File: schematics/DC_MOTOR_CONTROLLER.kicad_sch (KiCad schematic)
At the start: 0 parts

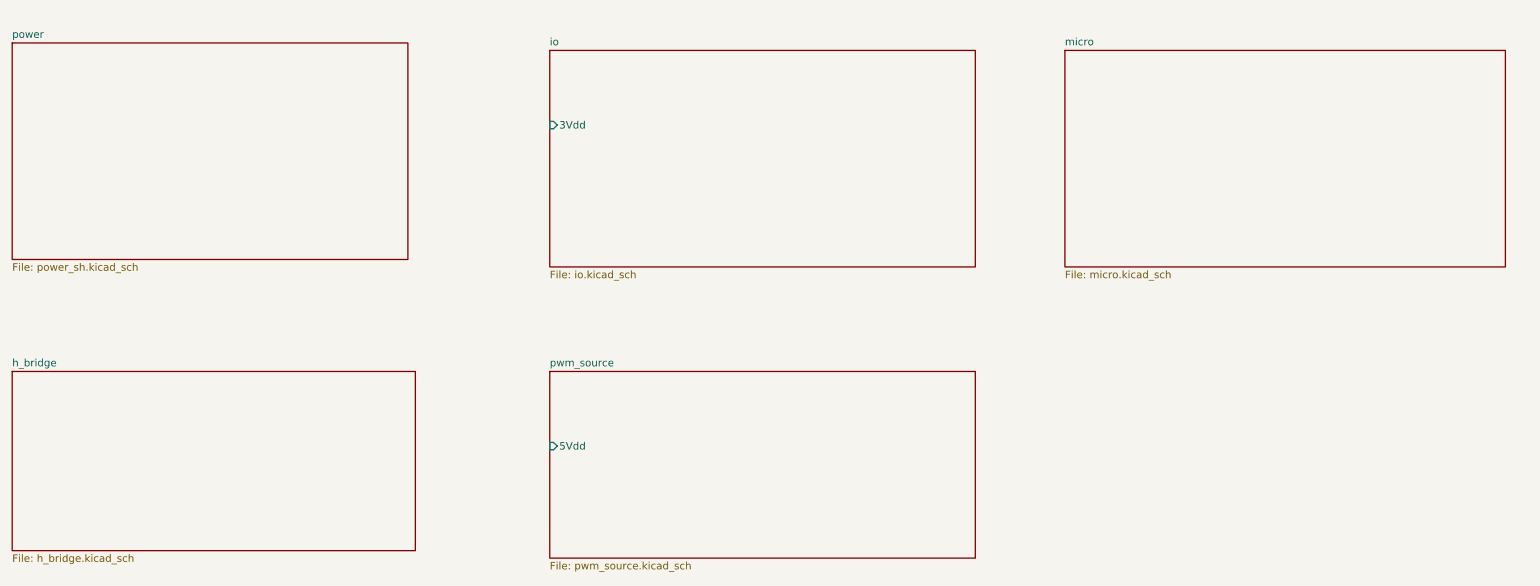
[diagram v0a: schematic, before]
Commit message: changed format to kicad project
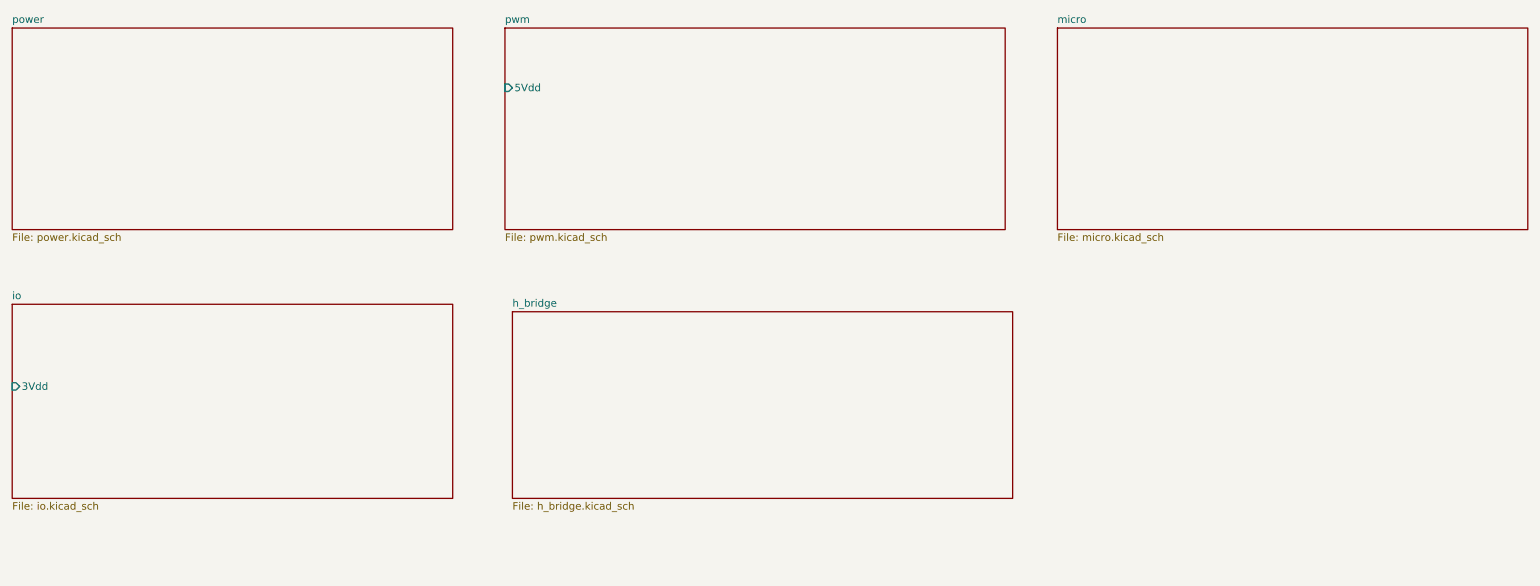
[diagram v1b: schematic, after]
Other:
- removed sheet pwm_source
- added sheet pwm (pwm.kicad_sch)
- sheet power: file power_sh.kicad_sch -> power.kicad_sch
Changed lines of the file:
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@@
 	(paper "A4")
 	(sheet
-		(at 20.32 21.59)
-		(size 67.31 36.83)
+		(at 105.41 67.31)
+		(size 85.09 31.75)
+		(exclude_from_sim no)
+		(in_bom yes)
+		(on_board yes)
+		(dnp no)
+		(fields_autoplaced yes)
+		(stroke
+			(width 0.1524)
+			(type solid)
+		)
+		(fill
+			(color 0 0 0 0.0000)
+		)
+		(property "Sheetname" "h_bridge"
+			(at 105.41 66.5984 0)
+			(effects
+				(font
+					(size 1.27 1.27)
+				)
+				(justify left bottom)
+			)
+		)
+		(property "Sheetfile" "h_bridge.kicad_sch"
+			(at 105.41 99.6446 0)
+			(effects
+				(font
+					(size 1.27 1.27)
+				)
+				(justify left top)
+			)
+		)
+		(instances
+			(project "DC_MOTOR_CONTROLLER"
+				(path "/047d9411-04a2-44fb-b408-2da9c75da8e5"
+					(page "6")
+				)
+			)
+		)
+	)
+	(sheet
+		(at 20.32 19.05)
+		(size 74.93 34.29)
 		(exclude_from_sim no)
 		(in_bom yes)
@@
 		)
 		(property "Sheetname" "power"
-			(at 20.32 20.8784 0)
-			(effects
-				(font
-					(size 1.27 1.27)
-				)
-				(justify left bottom)
-			)
-		)
-		(property "Sheetfile" "power_sh.kicad_sch"
-			(at 20.32 59.0046 0)
-			(effects
-				(font
-					(size 1.27 1.27)
-				)
-				(justify left top)
-			)
-		)
-		(instances
-			(project "DC_MOTOR_CONTROLLER"
-				(path "/4e267608-d3e9-4ae4-92d6-1e687cc2c969"
+			(at 20.32 18.3384 0)
+			(effects
+				(font
+					(size 1.27 1.27)
+				)
+				(justify left bottom)
+			)
+		)
+		(property "Sheetfile" "power.kicad_sch"
+			(at 20.32 53.9246 0)
+			(effects
+				(font
+					(size 1.27 1.27)
+				)
+				(justify left top)
+			)
+		)
+		(instances
+			(project "DC_MOTOR_CONTROLLER"
+				(path "/047d9411-04a2-44fb-b408-2da9c75da8e5"
 					(page "2")
 				)
@@
 	)
 	(sheet
-		(at 20.32 77.47)
-		(size 68.58 30.48)
-		(exclude_from_sim no)
-		(in_bom yes)
-		(on_board yes)
-		(dnp no)
-		(fields_autoplaced yes)
-		(stroke
-			(width 0.1524)
-			(type solid)
-		)
-		(fill
-			(color 0 0 0 0.0000)
-		)
-		(property "Sheetname" "h_bridge"
-			(at 20.32 76.7584 0)
-			(effects
-				(font
-					(size 1.27 1.27)
-				)
-				(justify left bottom)
-			)
-		)
-		(property "Sheetfile" "h_bridge.kicad_sch"
-			(at 20.32 108.5346 0)
-			(effects
-				(font
-					(size 1.27 1.27)
-				)
-				(justify left top)
-			)
-		)
-		(instances
-			(project "DC_MOTOR_CONTROLLER"
-				(path "/4e267608-d3e9-4ae4-92d6-1e687cc2c969"
+		(at 104.14 19.05)
+		(size 85.09 34.29)
+		(exclude_from_sim no)
+		(in_bom yes)
+		(on_board yes)
+		(dnp no)
+		(fields_autoplaced yes)
+		(stroke
+			(width 0.1524)
+			(type solid)
+		)
+		(fill
+			(color 0 0 0 0.0000)
+		)
+		(property "Sheetname" "pwm"
+			(at 104.14 18.3384 0)
+			(effects
+				(font
+					(size 1.27 1.27)
+				)
+				(justify left bottom)
+			)
+		)
+		(property "Sheetfile" "pwm.kicad_sch"
+			(at 104.14 53.9246 0)
+			(effects
+				(font
+					(size 1.27 1.27)
+				)
+				(justify left top)
+			)
+		)
+		(pin "5Vdd" input
+			(at 104.14 29.21 180)
+			(effects
+				(font
+					(size 1.27 1.27)
+				)
+				(justify left)
+			)
+		)
+		(instances
+			(project "DC_MOTOR_CONTROLLER"
+				(path "/047d9411-04a2-44fb-b408-2da9c75da8e5"
+					(page "3")
+				)
+			)
+		)
+	)
+	(sheet
+		(at 198.12 19.05)
+		(size 80.01 34.29)
+		(exclude_from_sim no)
+		(in_bom yes)
+		(on_board yes)
+		(dnp no)
+		(fields_autoplaced yes)
+		(stroke
+			(width 0.1524)
+			(type solid)
+		)
+		(fill
+			(color 0 0 0 0.0000)
+		)
+		(property "Sheetname" "micro"
+			(at 198.12 18.3384 0)
+			(effects
+				(font
+					(size 1.27 1.27)
+				)
+				(justify left bottom)
+			)
+		)
+		(property "Sheetfile" "micro.kicad_sch"
+			(at 198.12 53.9246 0)
+			(effects
+				(font
+					(size 1.27 1.27)
+				)
+				(justify left top)
+			)
+		)
+		(instances
+			(project "DC_MOTOR_CONTROLLER"
+				(path "/047d9411-04a2-44fb-b408-2da9c75da8e5"
+					(page "4")
+				)
+			)
+		)
+	)
+	(sheet
+		(at 20.32 66.04)
+		(size 74.93 33.02)
+		(exclude_from_sim no)
+		(in_bom yes)
+		(on_board yes)
+		(dnp no)
+		(fields_autoplaced yes)
+		(stroke
+			(width 0.1524)
+			(type solid)
+		)
+		(fill
+			(color 0 0 0 0.0000)
+		)
+		(property "Sheetname" "io"
+			(at 20.32 65.3284 0)
+			(effects
+				(font
+					(size 1.27 1.27)
+				)
+				(justify left bottom)
+			)
+		)
+		(property "Sheetfile" "io.kicad_sch"
+			(at 20.32 99.6446 0)
+			(effects
+				(font
+					(size 1.27 1.27)
+				)
+				(justify left top)
+			)
+		)
+		(pin "3Vdd" input
+			(at 20.32 80.01 180)
+			(effects
+				(font
+					(size 1.27 1.27)
+				)
+				(justify left)
+			)
+		)
+		(instances
+			(project "DC_MOTOR_CONTROLLER"
+				(path "/047d9411-04a2-44fb-b408-2da9c75da8e5"
 					(page "5")
 				)
 			)
-		)
-	)
-	(sheet
-		(at 111.76 22.86)
-		(size 72.39 36.83)
-		(exclude_from_sim no)
-		(in_bom yes)
-		(on_board yes)
-		(dnp no)
-		(fields_autoplaced yes)
-		(stroke
-			(width 0.1524)
-			(type solid)
-		)
-		(fill
-			(color 0 0 0 0.0000)
-		)
-		(property "Sheetname" "io"
-			(at 111.76 22.1484 0)
-			(effects
-				(font
-					(size 1.27 1.27)
-				)
-				(justify left bottom)
-			)
-		)
-		(property "Sheetfile" "io.kicad_sch"
-			(at 111.76 60.2746 0)
-			(effects
-				(font
-					(size 1.27 1.27)
-				)
-				(justify left top)
-			)
-		)
-		(pin "3Vdd" input
-			(at 111.76 35.56 180)
-			(effects
-				(font
-					(size 1.27 1.27)
-				)
-				(justify left)
-			)
-		)
-		(instances
-			(project "DC_MOTOR_CONTROLLER"
-				(path "/4e267608-d3e9-4ae4-92d6-1e687cc2c969"
-					(page "3")
-				)
-			)
-		)
-	)
-	(sheet
-		(at 199.39 22.86)
-		(size 74.93 36.83)
-		(exclude_from_sim no)
-		(in_bom yes)
-		(on_board yes)
-		(dnp no)
-		(fields_autoplaced yes)
-		(stroke
-			(width 0.1524)
-			(type solid)
-		)
-		(fill
-			(color 0 0 0 0.0000)
-		)
-		(property "Sheetname" "micro"
-			(at 199.39 22.1484 0)
-			(effects
-				(font
-					(size 1.27 1.27)
-				)
-				(justify left bottom)
-			)
-		)
-		(property "Sheetfile" "micro.kicad_sch"
-			(at 199.39 60.2746 0)
-			(effects
-				(font
-					(size 1.27 1.27)
-				)
-				(justify left top)
-			)
-		)
-		(instances
-			(project "DC_MOTOR_CONTROLLER"
-				(path "/4e267608-d3e9-4ae4-92d6-1e687cc2c969"
-					(page "4")
-				)
-			)
-		)
-	)
-	(sheet
-		(at 111.76 77.47)
-		(size 72.39 31.75)
-		(exclude_from_sim no)
-		(in_bom yes)
-		(on_board yes)
-		(dnp no)
-		(fields_autoplaced yes)
-		(stroke
-			(width 0.1524)
-			(type solid)
-		)
-		(fill
-			(color 0 0 0 0.0000)
-		)
-		(property "Sheetname" "pwm_source"
-			(at 111.76 76.7584 0)
-			(effects
-				(font
-					(size 1.27 1.27)
-				)
-				(justify left bottom)
-			)
-		)
-		(property "Sheetfile" "pwm_source.kicad_sch"
-			(at 111.76 109.8046 0)
-			(effects
-				(font
-					(size 1.27 1.27)
-				)
-				(justify left top)
-			)
-		)
-		(pin "5Vdd" input
-			(at 111.76 90.17 180)
-			(effects
-				(font
-					(size 1.27 1.27)
-				)
-				(justify left)
-			)
-		)
-		(instances
-			(project "DC_MOTOR_CONTROLLER"
-				(path "/4e267608-d3e9-4ae4-92d6-1e687cc2c969"
-					(page "6")
-				)
-			)
